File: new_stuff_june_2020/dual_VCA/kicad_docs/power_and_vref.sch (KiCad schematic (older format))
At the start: 26 parts, among them J7 power_input, U1 SSM2164, U2 TL072, U3 TL072, U4 TL072, U5 TL072, U6 MAX6035xxUR50

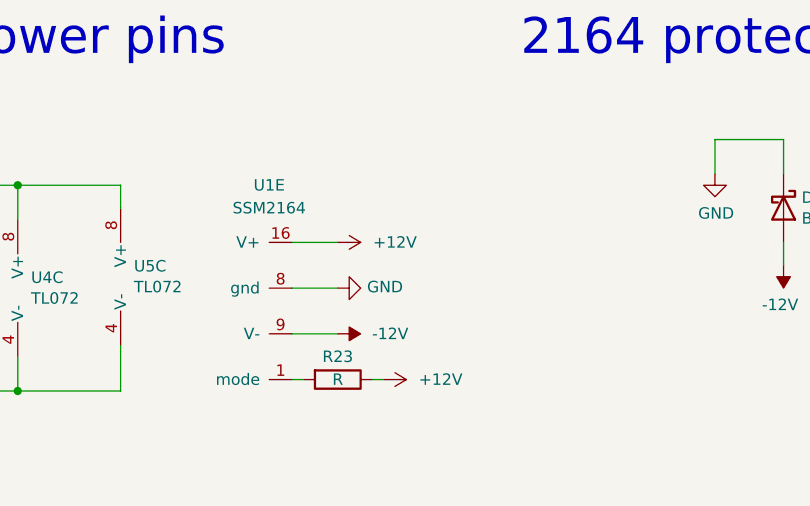
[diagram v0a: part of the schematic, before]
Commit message: add note about mode resistor
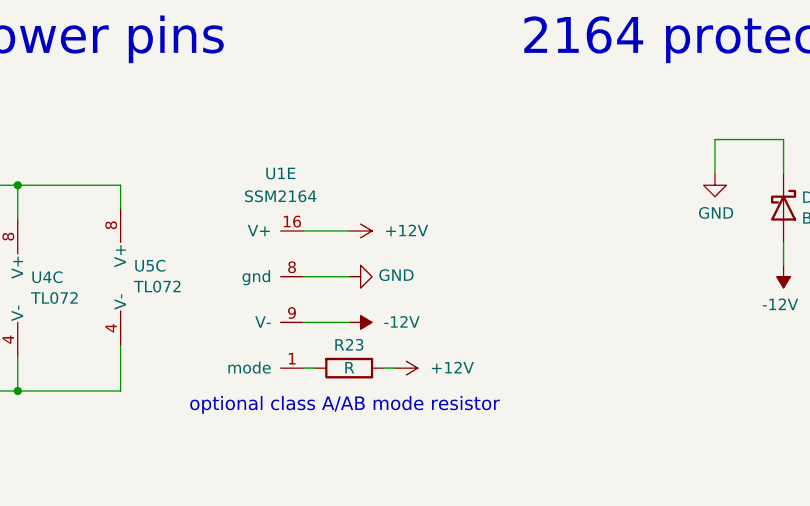
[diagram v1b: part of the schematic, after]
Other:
- note added: "optional class A/AB mode resistor"
- moved on the sheet: R23, U1E
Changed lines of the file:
@@
 L dual_VCA:SSM2164 U?
 U 5 1 5E6E7297
-P 8000 5500
+P 8050 5450
 AR Path="/5E6E7297" Ref="U?"  Part="5"
 AR Path="/5E6A7940/5E6E7297" Ref="U1"  Part="5"
-F 0 "U1" H 8000 5950 50  0000 C CNN
-F 1 "SSM2164" H 8000 5850 50  0000 C CNN
-F 2 "Package_DIP:DIP-16_W7.62mm" H 8100 5700 50  0001 C CNN
-F 3 "" H 8100 5700 50  0001 C CNN
-	5    8000 5500
+F 0 "U1" H 8050 5900 50  0000 C CNN
+F 1 "SSM2164" H 8050 5800 50  0000 C CNN
+F 2 "Package_DIP:DIP-16_W7.62mm" H 8150 5650 50  0001 C CNN
+F 3 "" H 8150 5650 50  0001 C CNN
+	5    8050 5450
 	1    0    0    -1
 $EndComp
@@
 L power:GND #PWR?
 U 1 1 5E6E7301
-P 8300 5500
+P 8350 5450
 AR Path="/5E6E7301" Ref="#PWR?"  Part="1"
 AR Path="/5E6A7940/5E6E7301" Ref="#PWR033"  Part="1"
-F 0 "#PWR033" H 8300 5250 50  0001 C CNN
-F 1 "GND" V 8305 5372 50  0000 R CNN
-F 2 "" H 8300 5500 50  0001 C CNN
-F 3 "" H 8300 5500 50  0001 C CNN
-	1    8300 5500
+F 0 "#PWR033" H 8350 5200 50  0001 C CNN
+F 1 "GND" V 8355 5322 50  0000 R CNN
+F 2 "" H 8350 5450 50  0001 C CNN
+F 3 "" H 8350 5450 50  0001 C CNN
+	1    8350 5450
 	0    -1   -1   0
 $EndComp
 Wire Wire Line
-	8300 5300 8100 5300
-Wire Wire Line
-	8300 5500 8100 5500
-Wire Wire Line
-	8300 5700 8100 5700
+	8350 5250 8150 5250
+Wire Wire Line
+	8350 5450 8150 5450
+Wire Wire Line
+	8350 5650 8150 5650
 $Comp
 L Device:R R?
 U 1 1 5E6E7316
-P 8300 5900
+P 8350 5850
 AR Path="/5E6E7316" Ref="R?"  Part="1"
 AR Path="/5E6A7940/5E6E7316" Ref="R23"  Part="1"
-F 0 "R23" V 8200 5900 50  0000 C CNN
-F 1 "R" V 8300 5900 50  0000 C CNN
-F 2 "Resistor_THT:R_Axial_DIN0207_L6.3mm_D2.5mm_P10.16mm_Horizontal" V 8230 5900 50  0001 C CNN
-F 3 "~" H 8300 5900 50  0001 C CNN
-	1    8300 5900
+F 0 "R23" V 8250 5850 50  0000 C CNN
+F 1 "R" V 8350 5850 50  0000 C CNN
+F 2 "Resistor_THT:R_Axial_DIN0207_L6.3mm_D2.5mm_P10.16mm_Horizontal" V 8280 5850 50  0001 C CNN
+F 3 "~" H 8350 5850 50  0001 C CNN
+	1    8350 5850
 	0    1    1    0
 $EndComp
 Wire Wire Line
-	8150 5900 8100 5900
-Wire Wire Line
-	8500 5900 8450 5900
+	8200 5850 8150 5850
+Wire Wire Line
+	8550 5850 8500 5850
 $Comp
 L power:GND #PWR?
@@
 L power:+12V #PWR0118
 U 1 1 5EEA2A59
-P 8300 5300
-F 0 "#PWR0118" H 8300 5150 50  0001 C CNN
-F 1 "+12V" V 8300 5550 50  0000 C CNN
-F 2 "" H 8300 5300 50  0001 C CNN
-F 3 "" H 8300 5300 50  0001 C CNN
-	1    8300 5300
+P 8350 5250
+F 0 "#PWR0118" H 8350 5100 50  0001 C CNN
+F 1 "+12V" V 8350 5500 50  0000 C CNN
+F 2 "" H 8350 5250 50  0001 C CNN
+F 3 "" H 8350 5250 50  0001 C CNN
+	1    8350 5250
 	0    1    1    0
 $EndComp
@@
 L power:+12V #PWR0119
 U 1 1 5EEBF084
-P 8500 5900
-F 0 "#PWR0119" H 8500 5750 50  0001 C CNN
-F 1 "+12V" V 8500 6150 50  0000 C CNN
-F 2 "" H 8500 5900 50  0001 C CNN
-F 3 "" H 8500 5900 50  0001 C CNN
-	1    8500 5900
+P 8550 5850
+F 0 "#PWR0119" H 8550 5700 50  0001 C CNN
+F 1 "+12V" V 8550 6100 50  0000 C CNN
+F 2 "" H 8550 5850 50  0001 C CNN
+F 3 "" H 8550 5850 50  0001 C CNN
+	1    8550 5850
 	0    1    1    0
 $EndComp
@@
 L power:-12V #PWR0123
 U 1 1 5EEC6739
-P 8300 5700
-F 0 "#PWR0123" H 8300 5800 50  0001 C CNN
-F 1 "-12V" V 8300 5850 50  0000 L CNN
-F 2 "" H 8300 5700 50  0001 C CNN
-F 3 "" H 8300 5700 50  0001 C CNN
-	1    8300 5700
+P 8350 5650
+F 0 "#PWR0123" H 8350 5750 50  0001 C CNN
+F 1 "-12V" V 8350 5800 50  0000 L CNN
+F 2 "" H 8350 5650 50  0001 C CNN
+F 3 "" H 8350 5650 50  0001 C CNN
+	1    8350 5650
 	0    1    1    0
 $EndComp
@@
 	-1   0    0    1
 $EndComp
+Text Notes 7650 6050 0    59   ~ 0
+optional class A/AB mode resistor
 $EndSCHEMATC

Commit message: generate BOMs for most boards
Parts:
- R23: value R -> opt
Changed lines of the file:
@@
 AR Path="/5E6A7940/5E6E7316" Ref="R23"  Part="1"
 F 0 "R23" V 8250 5850 50  0000 C CNN
-F 1 "R" V 8350 5850 50  0000 C CNN
+F 1 "opt" V 8350 5850 50  0000 C CNN
 F 2 "Resistor_THT:R_Axial_DIN0207_L6.3mm_D2.5mm_P10.16mm_Horizontal" V 8280 5850 50  0001 C CNN
 F 3 "~" H 8350 5850 50  0001 C CNN
